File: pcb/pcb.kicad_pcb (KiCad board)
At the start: 2 copper layers, 150 x 115 mm, 46 parts, among them J2 Conn_02x06_Odd_Even, J3 Conn_02x02_Odd_Even, U1 MCP3008, U2 MCP3008, U4 H11L1M

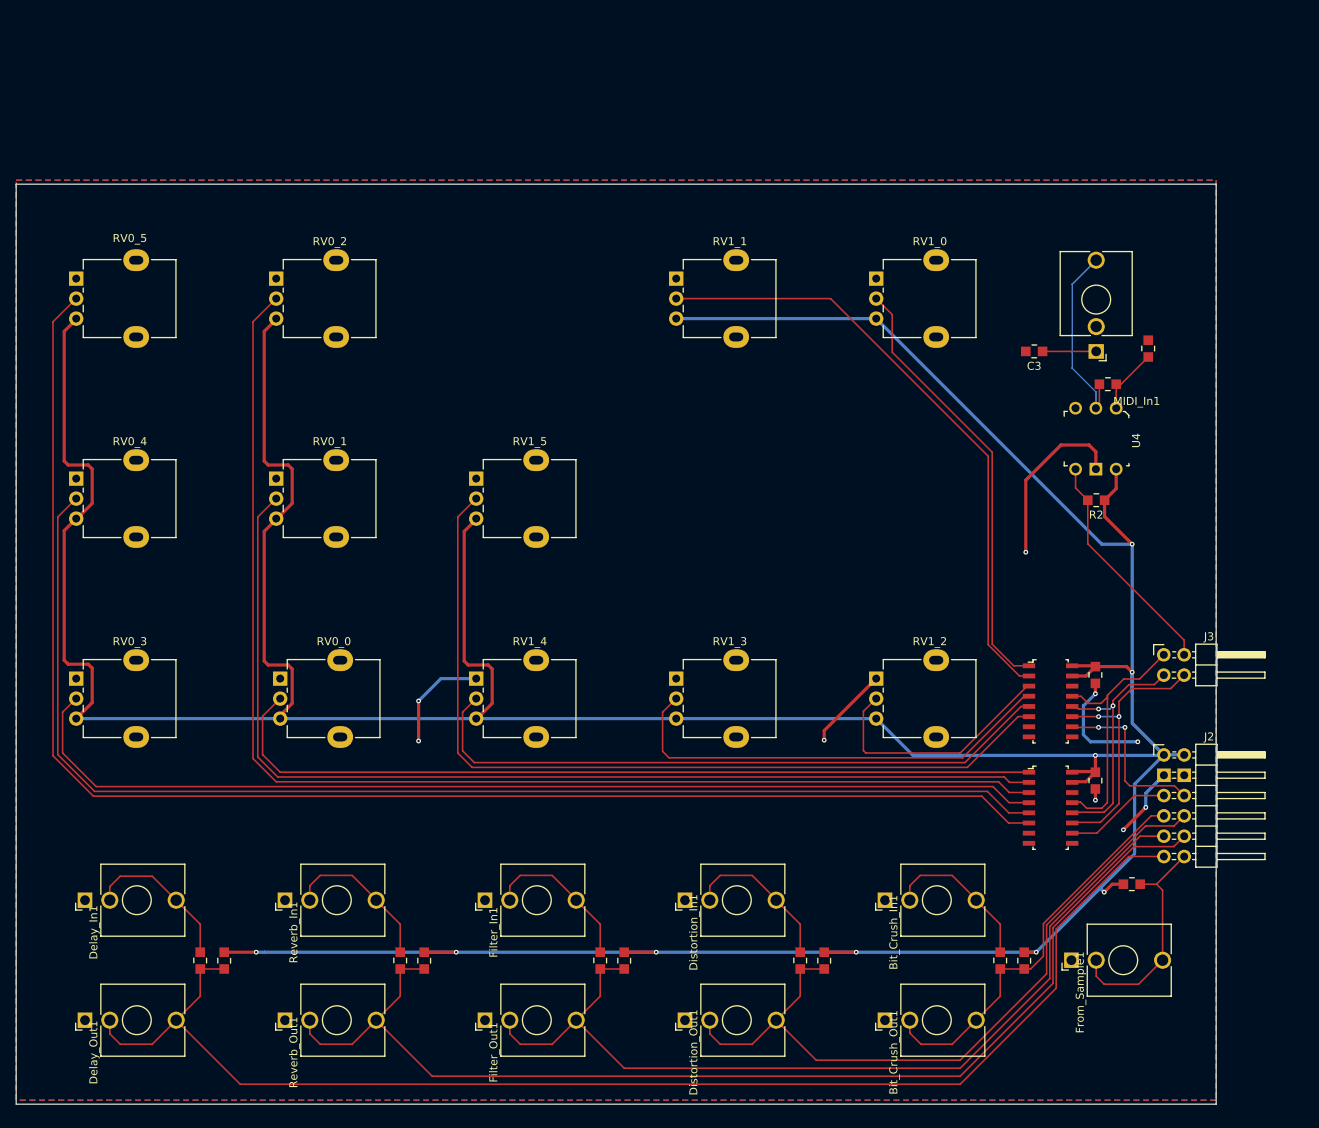
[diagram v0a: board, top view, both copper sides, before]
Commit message: finished pretty-ing up pcb layout
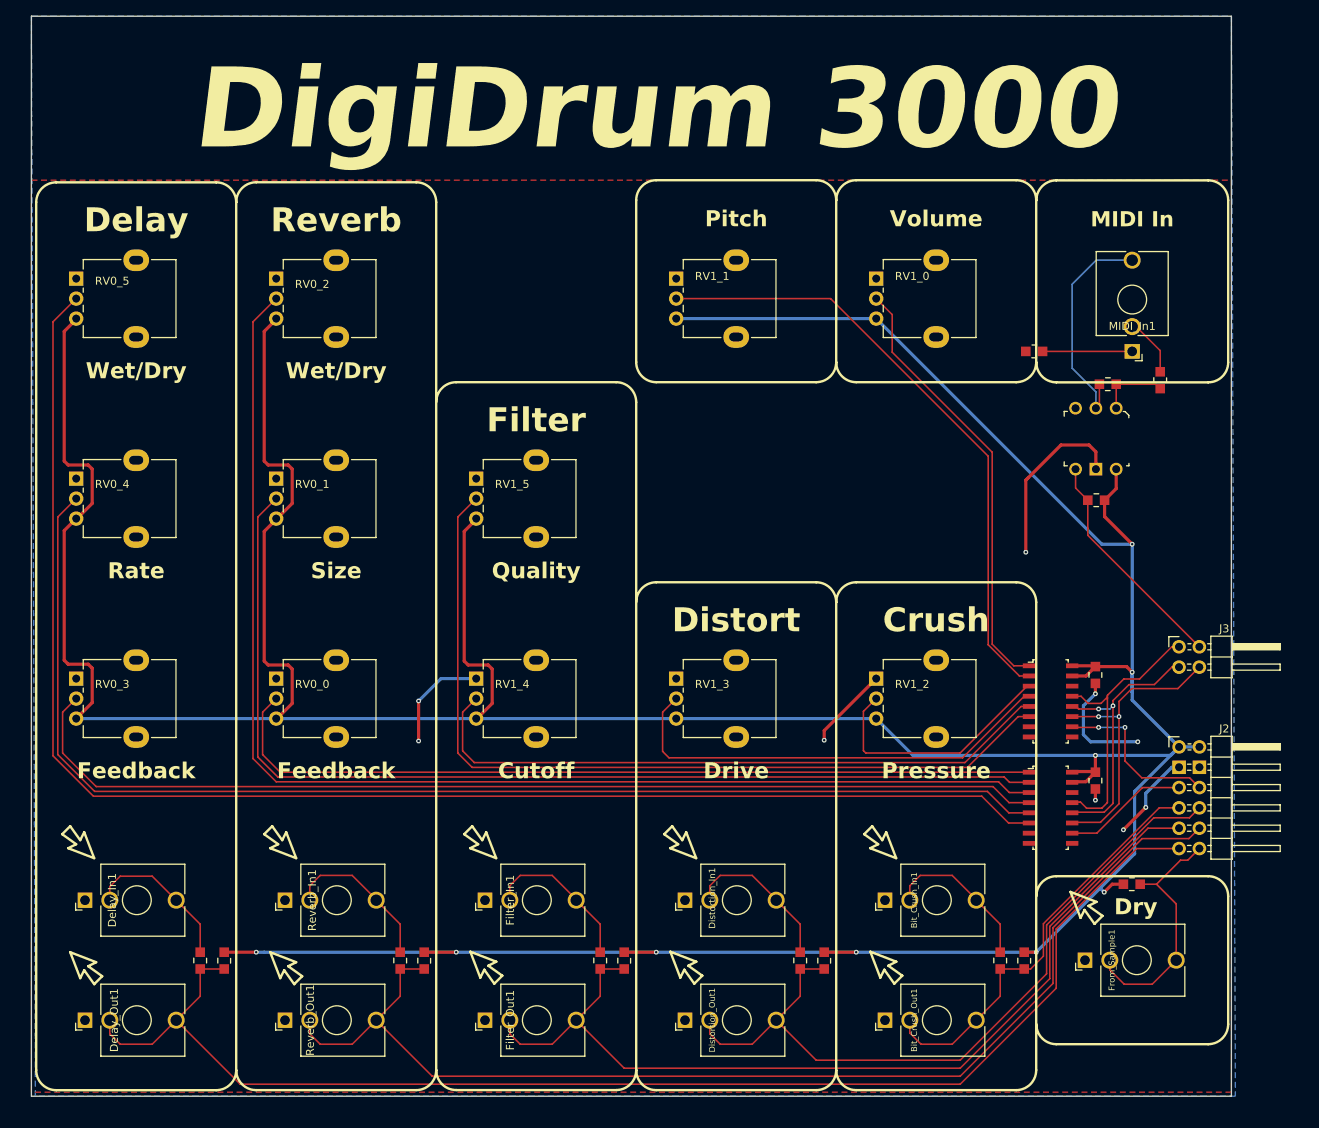
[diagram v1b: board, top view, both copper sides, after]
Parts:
- moved MIDI_In1 4.50 mm to (204.5, 66.4)
- moved R1 4.23 mm to (208.0, 70.0)
- moved J2 2.15 mm to (210.4, 115.8)
- moved J3 2.15 mm to (210.3, 103.3)
- moved From_Sample1 1.70 mm to (198.6, 142.5)
- moved RV0_0 0.50 mm to (97.5, 107.3)
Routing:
- net Net-(MIDI_In1-PadR): track 0.00 -> 6.89 mm
- net Net-(D3-A): track 24.2 -> 29.2 mm
- net Net-(C3-Pad1): track 6.70 -> 11.7 mm
- net +3.3V: track 567.7 -> 571.5 mm
- net Net-(J2-Pin_12): track 28.7 -> 31.3 mm
- net Net-(D2-A): track 142.8 -> 145.1 mm
- net GND: track 70.4 -> 72.7 mm
- net Net-(J3-Pin_3): track 31.5 -> 33.8 mm
- net Net-(J2-Pin_5): track 13.4 -> 15.7 mm
- net Net-(J3-Pin_1): track 32.9 -> 35.2 mm
- net Net-(D5-A): track 114.2 -> 116.5 mm
- net Net-(D4-A): track 50.2 -> 52.5 mm
- net Net-(D1-A): track 165.3 -> 167.6 mm
- net Net-(J3-Pin_4): track 35.0 -> 37.3 mm
- net Net-(D6-A): track 91.7 -> 94.0 mm
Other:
- board size 150 x 115 mm -> 150 x 135 mm
- board text added: "Crush"
- board text added: "Cutoff"
- board text added: "Delay"
- board text added: "DigiDrum 3000"
- board text added: "Distort"
- board text added: "Drive"
- board text added: "Dry"
- board text added: "Feedback"
- board text added: "Filter"
- board text added: "MIDI In"
- board text added: "Pitch"
- board text added: "Pressure"
- board text added: "Quality"
- board text added: "Rate"
- board text added: "Reverb"
- board text added: "Size"
- board text added: "Volume"
- board text added: "Wet/Dry"

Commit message: updated pcb based on schottky diodes availible from lab on floor 5
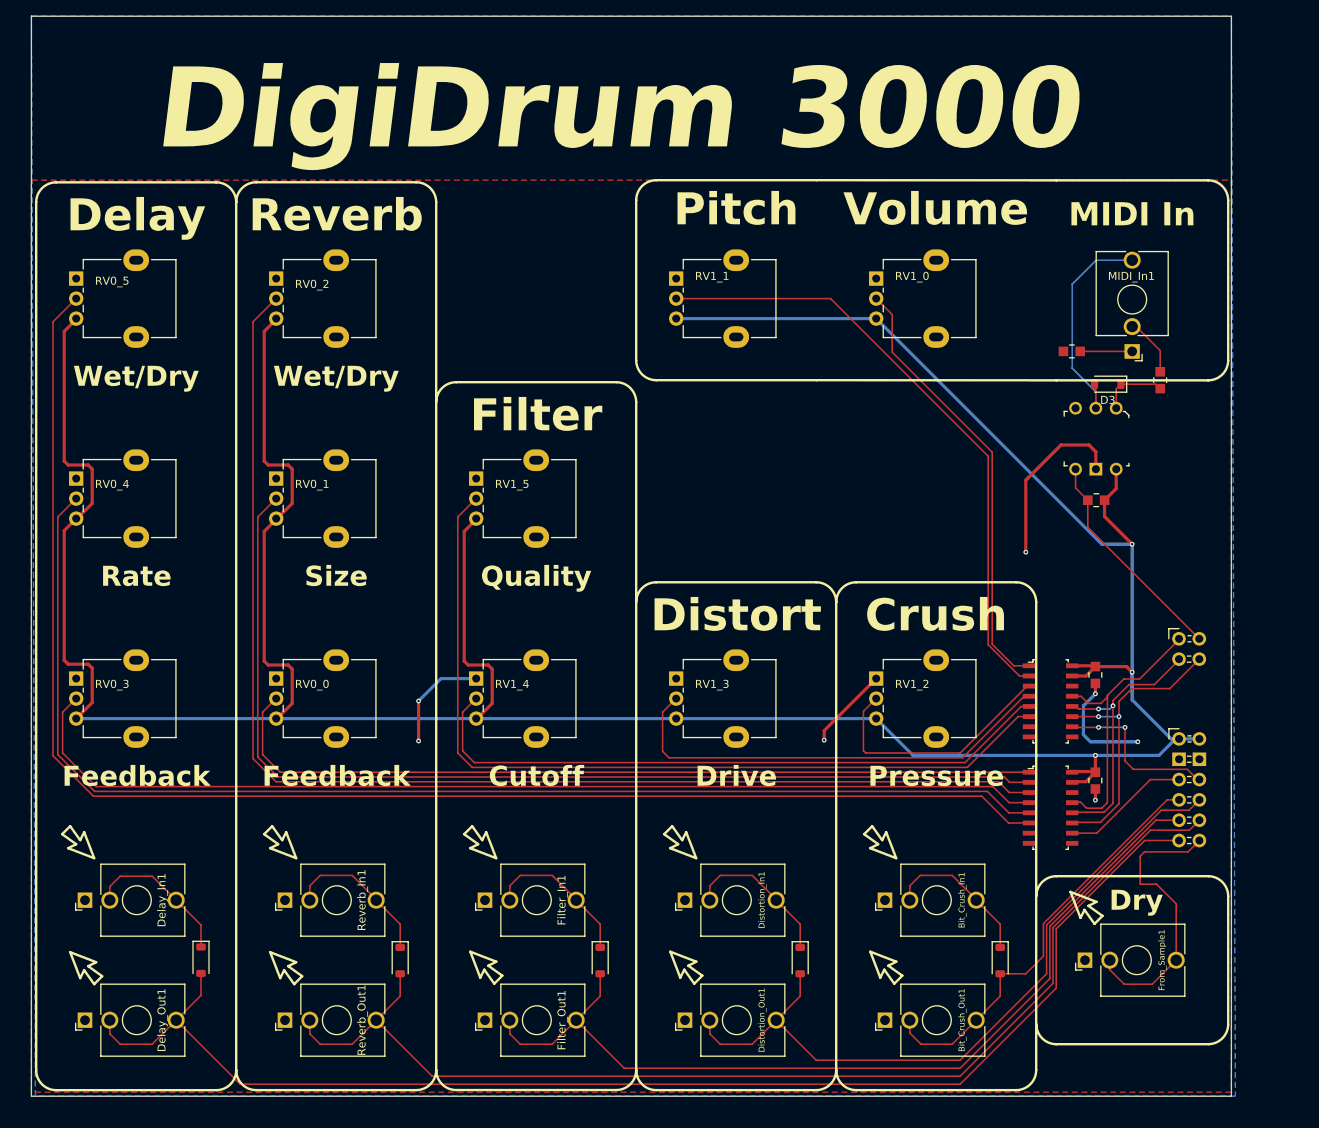
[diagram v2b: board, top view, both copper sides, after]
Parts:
- removed R3, R4, R5, R6, R7, R8: 4.7k, digikey-footprints:0805
- D1, D2, D3, D4, D5, D6: value D -> BAT46ZFILM; footprint digikey-footprints:0805 -> Diode_SMD:D_SOD-123
- moved C3 4.70 mm to (196.9, 66.4)
- moved J2 1.00 mm to (210.4, 114.8)
- moved J3 1.00 mm to (210.3, 102.3)
- moved D1 0.11 mm to (88.1, 142.5)
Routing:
- net +3.3V: track 571.5 -> 420.0 mm, vias 9 -> 3
- net GND: track 72.7 -> 61.5 mm, vias 9 -> 7
- net Net-(C3-Pad1): track 11.7 -> 6.64 mm
- net Net-(J2-Pin_12): track 31.3 -> 35.8 mm
- net Net-(D5-A): track 116.5 -> 112.3 mm
- net Net-(D6-A): track 94.0 -> 90.8 mm
- net Net-(D2-A): track 145.1 -> 142.0 mm
- net Net-(D1-A): track 167.6 -> 164.5 mm
- net Net-(J3-Pin_2): track 28.6 -> 27.6 mm
- net Net-(D1-K): track 19.5 -> 18.9 mm
- net Net-(D6-K): track 19.5 -> 18.9 mm
- net Net-(D5-K): track 19.5 -> 18.9 mm
- net Net-(D4-K): track 19.5 -> 18.9 mm
- net Net-(D2-K): track 19.5 -> 18.9 mm

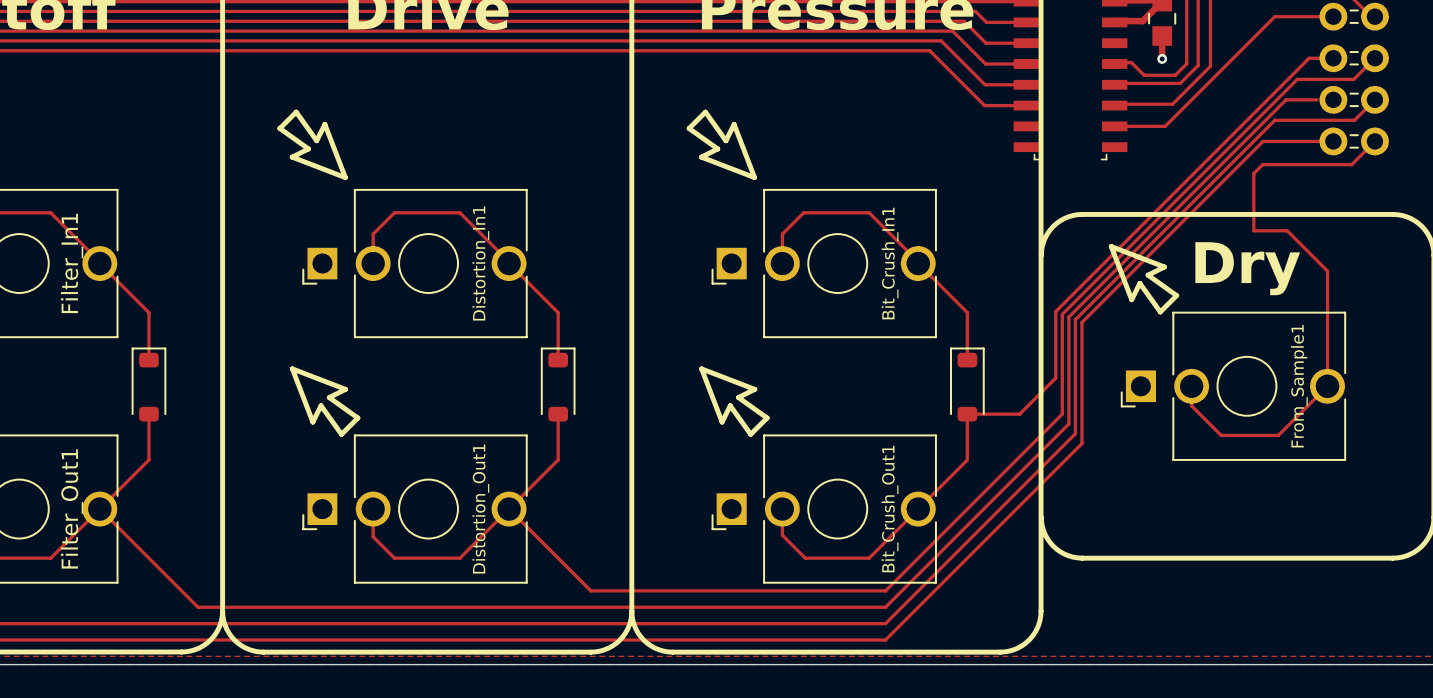
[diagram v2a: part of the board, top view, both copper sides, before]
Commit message: fixed my mistake THAT I COULD HAVE CAUGHT WITH DRC that seperates a trace from the pins by .1mm
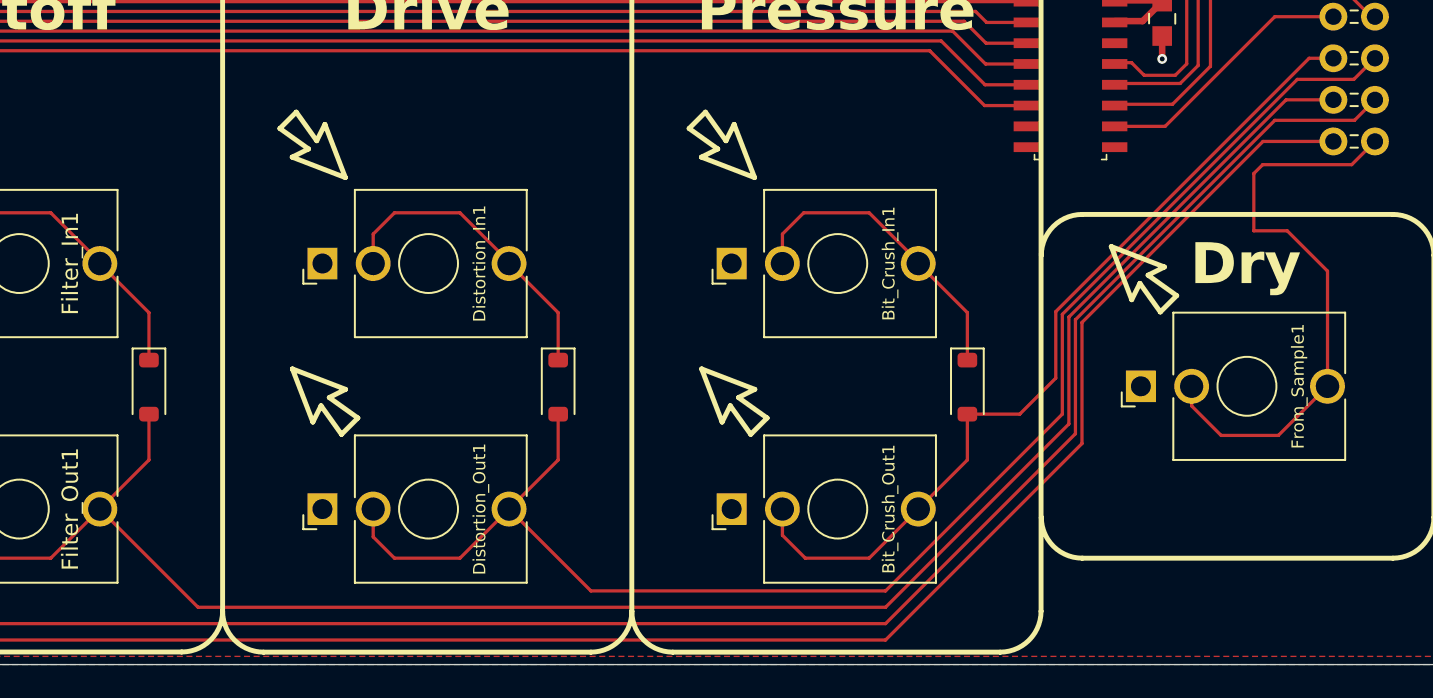
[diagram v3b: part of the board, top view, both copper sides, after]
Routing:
- net Net-(D5-A): track 112.3 -> 113.3 mm
